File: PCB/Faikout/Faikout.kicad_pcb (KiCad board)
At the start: 2 copper layers, 70 x 70 mm, 47 parts, among them J1 1x5, J2 TC2030-USB-NL, J3 Reset, Q1 BSS138PS, U1 TPS562246, U4 ESP32-S3-MINI-1-N4R2

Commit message: Started on POE
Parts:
- J1: value 1x5 -> S21
- U4: value ESP32-S3-MINI-1-N4R2 -> ESP32-S3-MINI-1

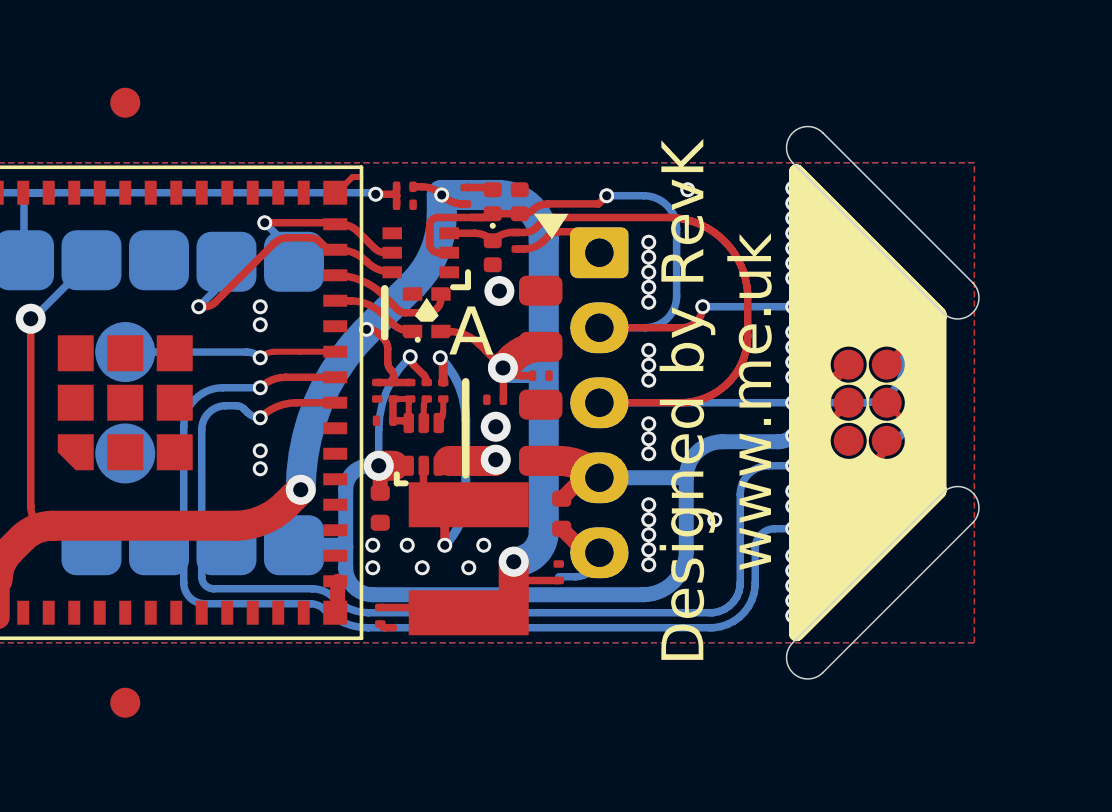
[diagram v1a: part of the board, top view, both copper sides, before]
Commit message: New regulator
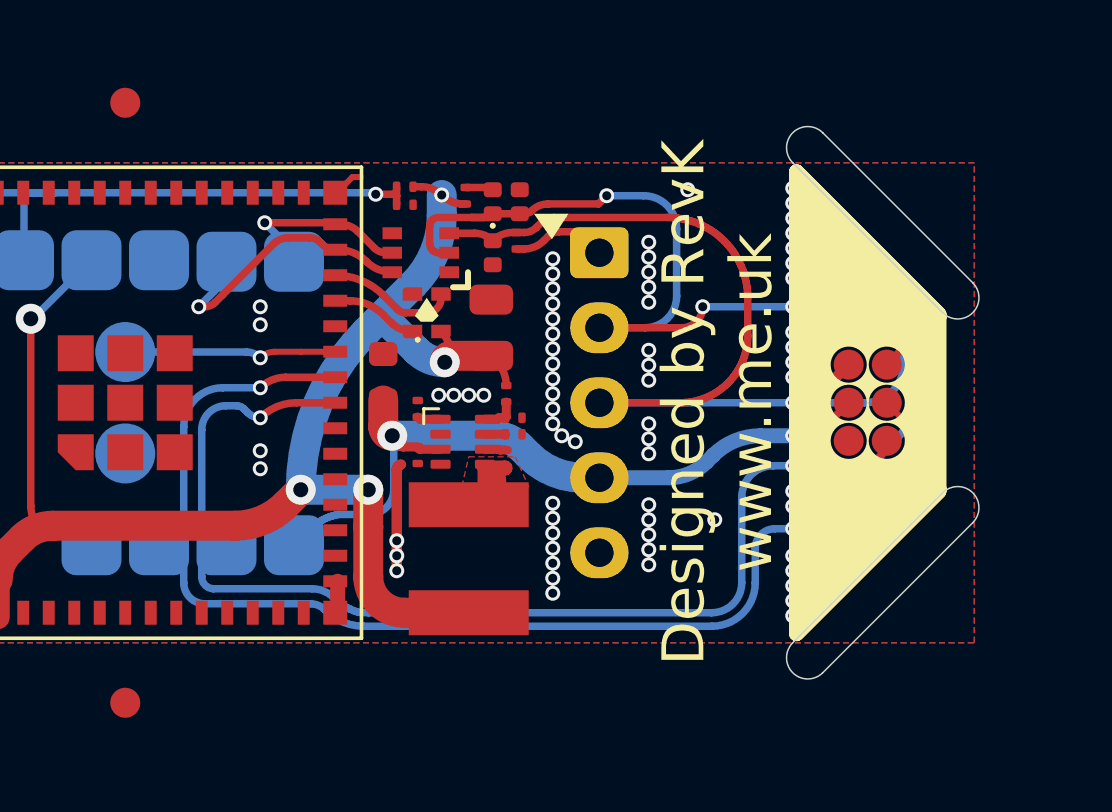
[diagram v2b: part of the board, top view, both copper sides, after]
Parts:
- removed C1, C18, C2, C4, C5, C7: 100nF, RevK:C_0201
- removed C15: 47uF 6V3, RevK:C_0805
- removed C16, C3: 100nF 25V, RevK:C_0402
- removed C17: 22uF 25V, RevK:C_0805
- removed C19: 18pF, RevK:C_0201
- removed L1: 4.7uH, RevK:L_5x5
- removed R5, R6: 150k 1%, RevK:R_0201
- removed R8: 33k 1%, RevK:R_0201
- removed U1: TPS562246, RevK:SOT-5x3-6
- added C29: 10uF 35V, RevK:C_0603, F.Cu at (138.3, 64.2)
- added C30: 100nF 35V, RevK:C_0201, F.Cu at (139.5, 66.8)
- added C31: 33nF, RevK:C_0201, F.Cu at (142.7, 66.0)
- added C32: 100nF 35V, RevK:C_0201, F.Cu at (142.4, 66.8)
- added C33: 100uF 6.3V, RevK:C_0805, F.Cu at (141.9, 62.5)
- added L13: 4.7uH, RevK:L_5x5, F.Cu at (141.2, 70.2)
- added R15: 33k, RevK:R_0201, F.Cu at (139.5, 65.2)
- added R16: 30.9k 1%, RevK:R_0201, F.Cu at (142.4, 64.7)
- added R17: 10k, RevK:R_0201, F.Cu at (142.7, 65.5)
- added U5: TPS62933, RevK:SOT-583-8, F.Cu at (141.0, 66.3)
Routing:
- net +3.3V: track 66.6 -> 50.8 mm, vias 6 -> 5
- net DC: track 40.6 -> 26.3 mm, vias 3 -> 2
- net SW: track 9.82 -> 3.65 mm, vias 2 -> 0
- net FB: track 2.64 -> 1.24 mm
- net GND: track 7.01 -> 5.63 mm, vias 72 -> 91
- net EN: track 0.83 -> 0.00 mm
- net RT: track 0.00 -> 0.79 mm
- net SS: track 0.00 -> 0.69 mm
- added copper zone on F.Cu, net SW
